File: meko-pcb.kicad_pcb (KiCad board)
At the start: 2 copper layers, 4 parts, among them IC1 ES9218PQ, U1 ESP32-MINI-1, U2 CP2102N-Axx-xQFN28, U4 CP2102N-Axx-xQFN20

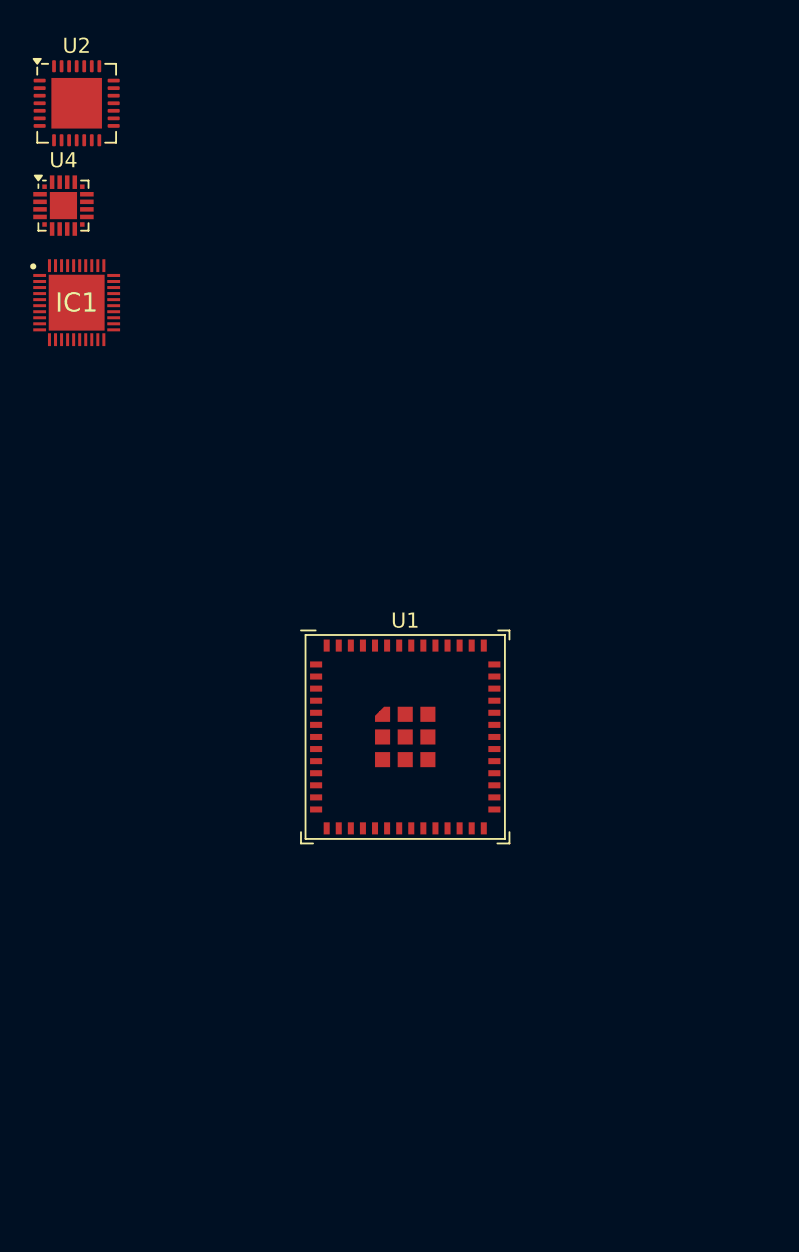
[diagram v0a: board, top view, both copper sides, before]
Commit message: added hall effect encoder
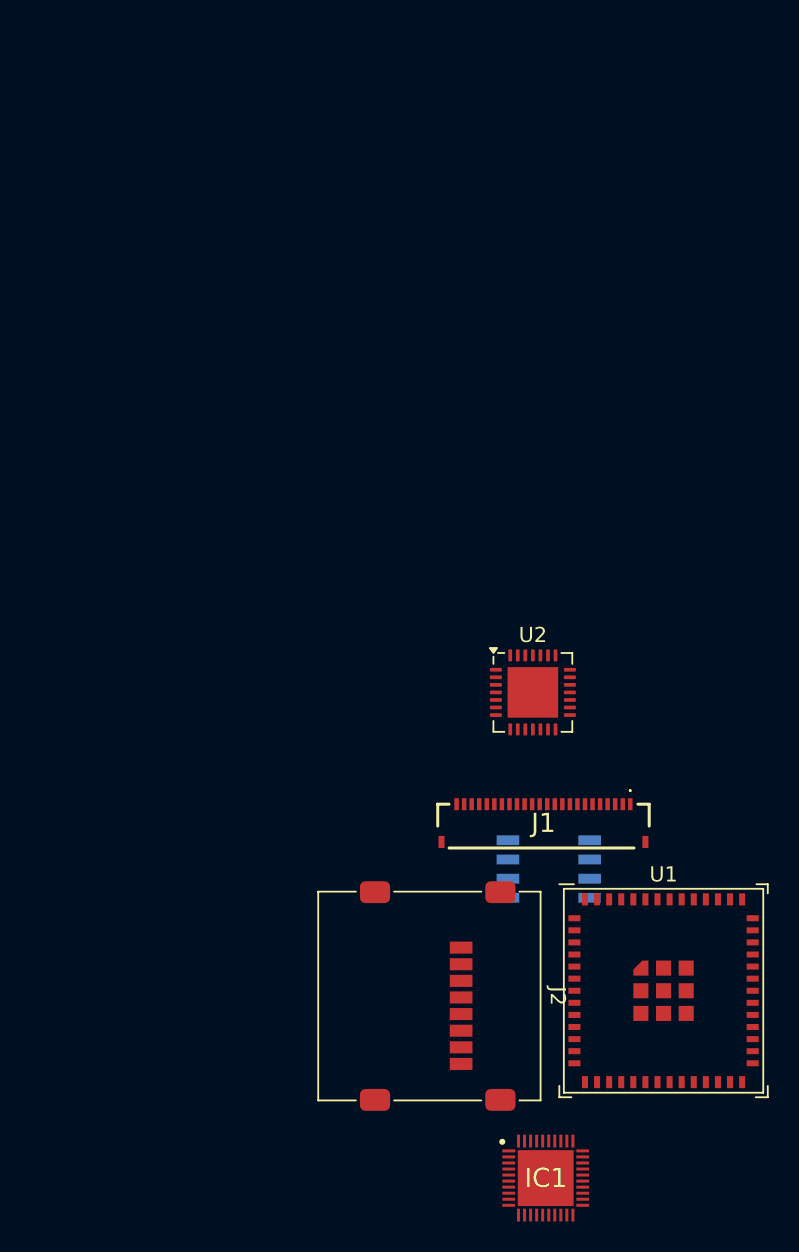
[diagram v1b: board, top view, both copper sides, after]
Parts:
- removed U4: CP2102N-Axx-xQFN20, Package_DFN_QFN:SiliconLabs_QFN-20-1EP_3x3mm_P0.5mm_EP1.8x1.8mm
- added IC2: AS5600-ASOM, AS5600-ASOM:SOIC127P600X175-8N, B.Cu at (166.3, 120.2)
- added J1: FH34SRJ-24S-0.5SH_99_, FH34SRJ-24S-0.5SH(99):FH34SRJ24S05SH99, F.Cu at (165.9, 117.3)
- added J2: Micro_SD_Card, Connector_Card:microSD_HC_Molex_47219-2001, F.Cu at (158.4, 128.6)
- IC1: footprint footprint:QFN40P500X500X80-41N-D -> ES9218PQ:QFN40P500X500X80-41N-D
- moved IC1 65.7 mm to (166.1, 140.7)
- moved U2 49.3 mm to (165.2, 108.5)
- moved U1 24.0 mm to (173.9, 128.2)

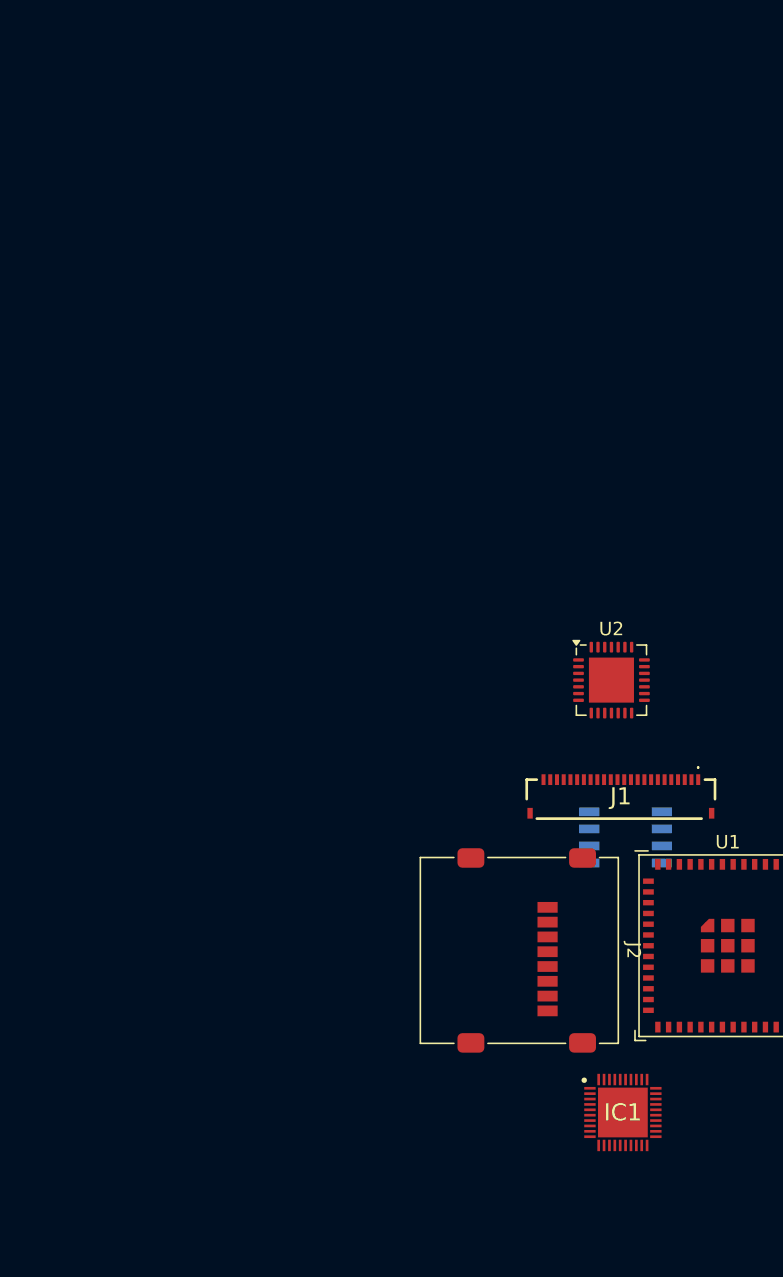
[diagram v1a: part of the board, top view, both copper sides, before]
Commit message: changed the switch converter to a LDOs
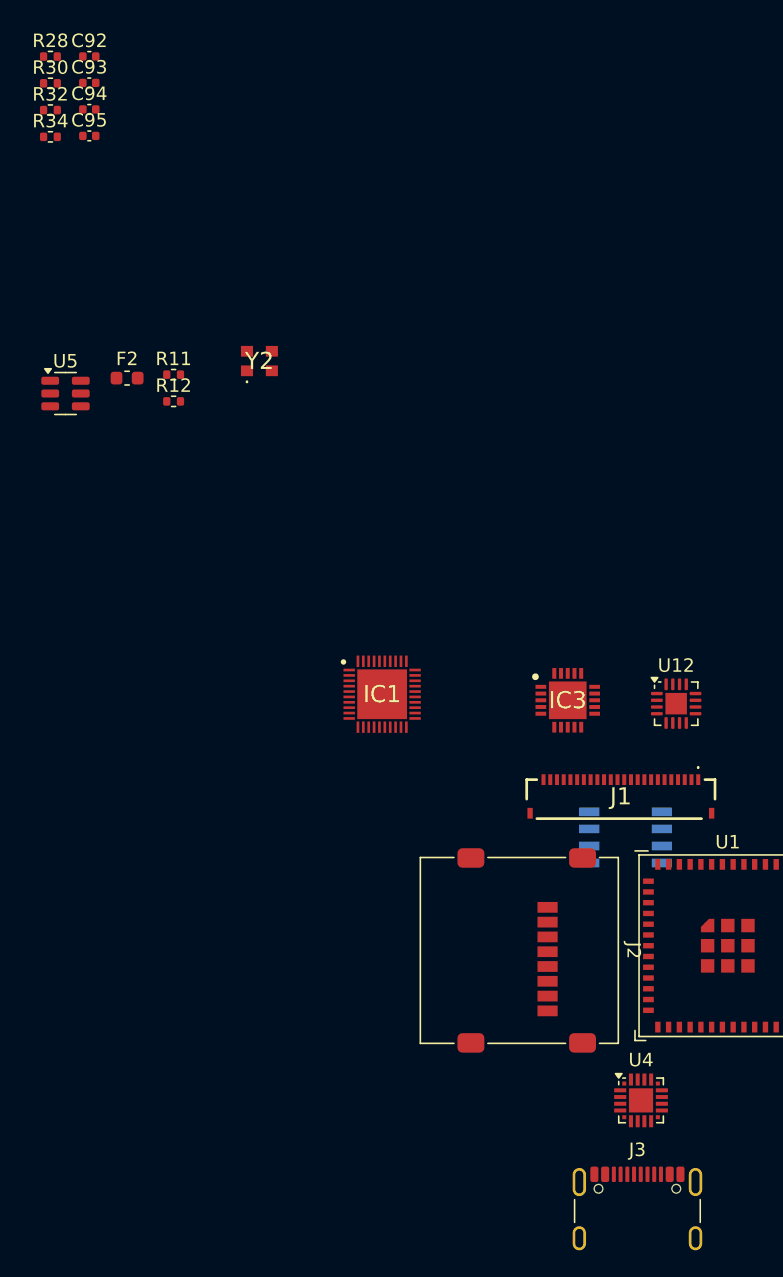
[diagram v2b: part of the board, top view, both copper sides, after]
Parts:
- removed U2: CP2102N-Axx-xQFN28, Package_DFN_QFN:QFN-28-1EP_5x5mm_P0.5mm_EP3.35x3.35mm
- added C92: 4.7uF, Capacitor_SMD:C_0402_1005Metric, F.Cu at (126.4, 62.1)
- added C93: 4.7uF, Capacitor_SMD:C_0402_1005Metric, F.Cu at (126.4, 64.1)
- added C94: 4.7uF, Capacitor_SMD:C_0402_1005Metric, F.Cu at (126.4, 66.1)
- added C95: 4.7uF, Capacitor_SMD:C_0402_1005Metric, F.Cu at (126.4, 68.0)
- added F2: 500mA, Fuse:Fuse_0603_1608Metric, F.Cu at (129.2, 86.0)
- added IC3: TPS7A8701RTJT, TPS7A8701RTJT:QFN50P400X400X80-21N-D, F.Cu at (162.0, 110.0)
- added J3: USB_C_Receptacle_USB2.0_16P, Connector_USB:USB_C_Receptacle_GCT_USB4105-xx-A_16P_TopMnt_Horizontal, F.Cu at (167.2, 148.9)
- added R11: 5.1k, Resistor_SMD:R_0402_1005Metric, F.Cu at (132.7, 85.8)
- added R12: 5.1k, Resistor_SMD:R_0402_1005Metric, F.Cu at (132.7, 87.8)
- added R28: 1.7k, Resistor_SMD:R_0402_1005Metric, F.Cu at (123.5, 62.1)
- added R30: 1.5k, Resistor_SMD:R_0402_1005Metric, F.Cu at (123.5, 64.1)
- added R32: 47k, Resistor_SMD:R_0402_1005Metric, F.Cu at (123.5, 66.1)
- added R34: 10k, Resistor_SMD:R_0402_1005Metric, F.Cu at (123.5, 68.1)
- added U12: BQ24075RGT, Package_DFN_QFN:VQFN-16-1EP_3x3mm_P0.5mm_EP1.6x1.6mm, F.Cu at (170.1, 110.2)
- added U4: CP2102N-Axx-xQFN20, Package_DFN_QFN:SiliconLabs_QFN-20-1EP_3x3mm_P0.5mm_EP1.8x1.8mm, F.Cu at (167.4, 139.8)
- added U5: USBLC6-2SC6, Package_TO_SOT_SMD:SOT-23-6, F.Cu at (124.7, 87.2)
- added Y2: ECS-2520SMV-500-GP-TR, ECS-2520SMV-500-GP-TR:ECS2520SMV500GPTR, F.Cu at (139.1, 84.8)
- moved IC1 35.9 mm to (148.2, 109.5)
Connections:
- IC1 pad 1: unconnected-(IC1-RT1-Pad1) -> GND
- IC1 pad 10: unconnected-(IC1-GSN_R-Pad10) -> GND
- IC1 pad 11: unconnected-(IC1-AGND_2-Pad11) -> GND
- IC1 pad 12: unconnected-(IC1-AGND_3-Pad12) -> GND
- IC1 pad 13: unconnected-(IC1-PNEG-Pad13) -> /audio/PNEG
- IC1 pad 14: unconnected-(IC1-PNEG_VC-Pad14) -> /audio/PNEG_VC
- IC1 pad 15: unconnected-(IC1-C2-Pad15) -> /audio/C2
- IC1 pad 16: unconnected-(IC1-C2_VC-Pad16) -> /audio/C2_VC
- IC1 pad 17: unconnected-(IC1-C1_VC-Pad17) -> /audio/C1_VC
- IC1 pad 18: unconnected-(IC1-C1-Pad18) -> /audio/C1
- IC1 pad 19: unconnected-(IC1-AVCC18-Pad19) -> +1V8
- IC1 pad 20: unconnected-(IC1-AVCC33-Pad20) -> +3V3
- IC1 pad 21: unconnected-(IC1-GSN_L-Pad21) -> GND
- IC1 pad 22: unconnected-(IC1-OUT_L-Pad22) -> Net-(IC1-OUT_L)
- IC1 pad 23: unconnected-(IC1-IN_L-Pad23) -> Net-(IC1-IN_L)
- IC1 pad 24: unconnected-(IC1-INB_L-Pad24) -> Net-(IC1-INB_L)
- IC1 pad 26: unconnected-(IC1-AGND_4-Pad26) -> GND
- IC1 pad 27: unconnected-(IC1-AVCC_DAC-Pad27) -> /audio/AVCC_DAC
- IC1 pad 28: unconnected-(IC1-VREF-Pad28) -> /audio/VREF
- IC1 pad 29: unconnected-(IC1-AVDD-Pad29) -> +1V8
- IC1 pad 3: unconnected-(IC1-XI-Pad3) -> /audio/XI
- IC1 pad 30: unconnected-(IC1-DGND_1-Pad30) -> GND
- IC1 pad 31: unconnected-(IC1-DVDD-Pad31) -> /audio/DVDD
- IC1 pad 4: unconnected-(IC1-VCCA-Pad4) -> +3V3
- IC1 pad 40: unconnected-(IC1-ADDR-Pad40) -> GND
- IC1 pad 41: unconnected-(IC1-DGND_2-Pad41) -> GND
- IC1 pad 5: unconnected-(IC1-AGND_1-Pad5) -> GND
- IC1 pad 7: unconnected-(IC1-INB_R-Pad7) -> Net-(IC1-INB_R)
- IC1 pad 8: unconnected-(IC1-IN_R-Pad8) -> Net-(IC1-IN_R)
- IC1 pad 9: unconnected-(IC1-OUT_R-Pad9) -> Net-(IC1-OUT_R)
- U1 pad 1: Net-(U1-GND-Pad1) -> GND
- U1 pad 2: Net-(U1-GND-Pad1) -> GND
- U1 pad 27: Net-(U1-GND-Pad1) -> GND
- U1 pad 38: Net-(U1-GND-Pad1) -> GND
- U1 pad 39: Net-(U1-GND-Pad1) -> GND
- U1 pad 40: Net-(U1-GND-Pad1) -> GND
- U1 pad 41: Net-(U1-GND-Pad1) -> GND
- U1 pad 42: Net-(U1-GND-Pad1) -> GND
- U1 pad 43: Net-(U1-GND-Pad1) -> GND
- U1 pad 44: Net-(U1-GND-Pad1) -> GND
- U1 pad 45: Net-(U1-GND-Pad1) -> GND
- U1 pad 46: Net-(U1-GND-Pad1) -> GND
- U1 pad 47: Net-(U1-GND-Pad1) -> GND
- U1 pad 48: Net-(U1-GND-Pad1) -> GND
- U1 pad 49: Net-(U1-GND-Pad1) -> GND
- U1 pad 50: Net-(U1-GND-Pad1) -> GND
- U1 pad 51: Net-(U1-GND-Pad1) -> GND
- U1 pad 52: Net-(U1-GND-Pad1) -> GND
- U1 pad 53: Net-(U1-GND-Pad1) -> GND
- U1 pad 54: Net-(U1-GND-Pad1) -> GND
- U1 pad 55: Net-(U1-GND-Pad1) -> GND

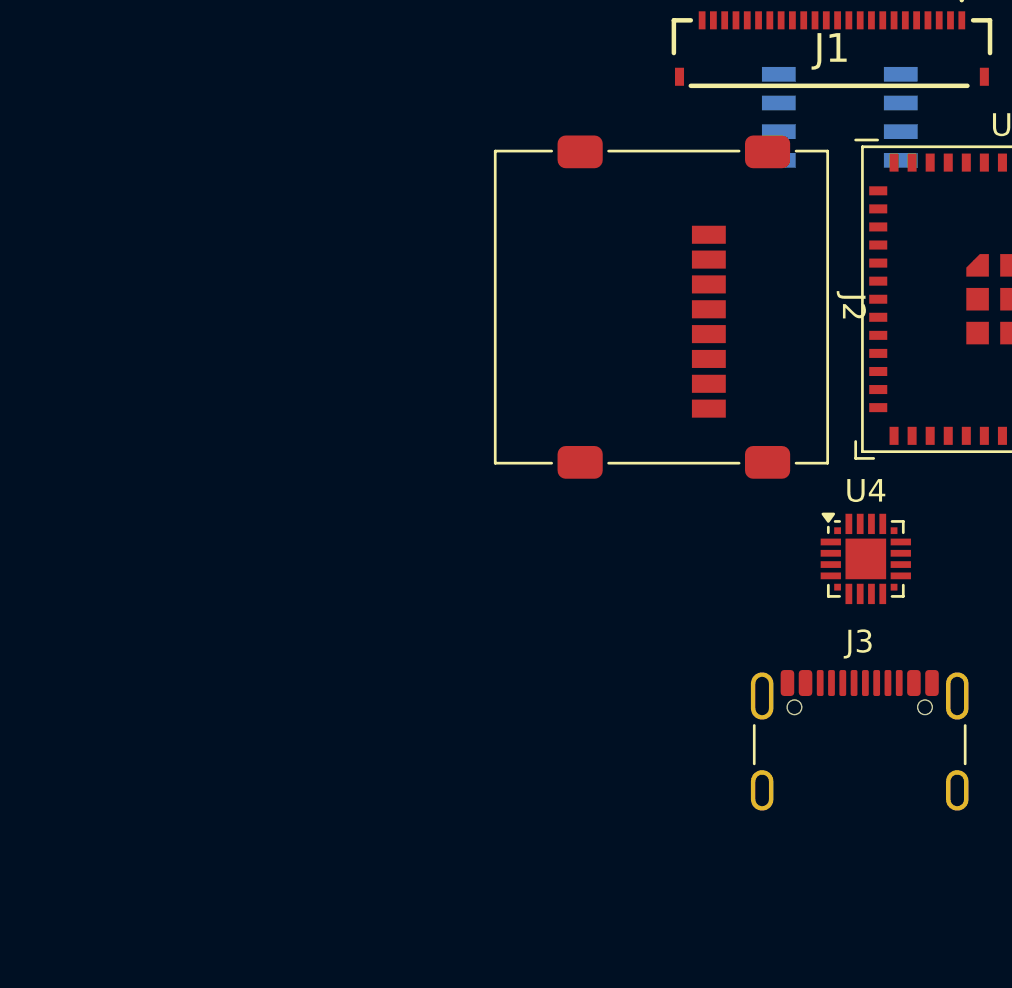
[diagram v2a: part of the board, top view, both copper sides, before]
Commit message: added the sd card slot
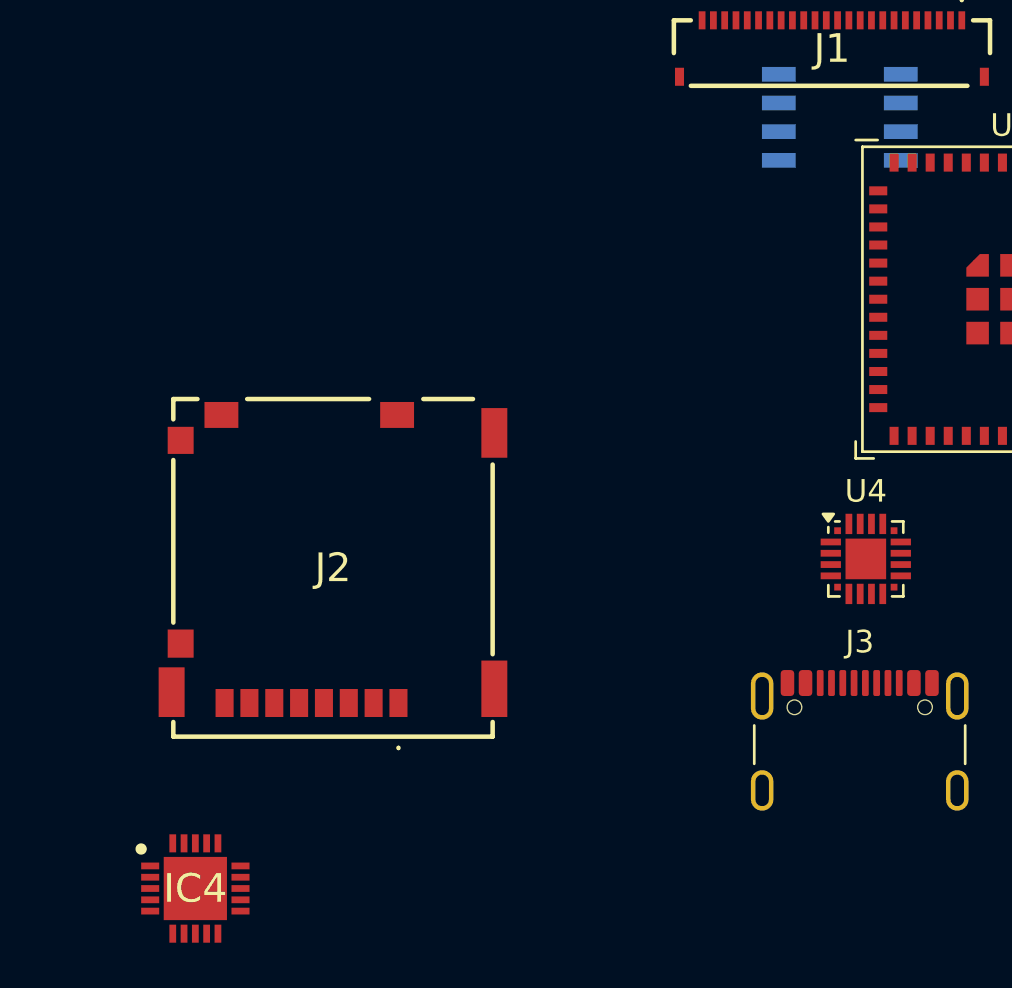
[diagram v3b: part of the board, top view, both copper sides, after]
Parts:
- added IC4: TPS7A8701RTJT, TPS7A8701RTJT:QFN50P400X400X80-21N-D, F.Cu at (137.8, 154.3)
- J2: value Micro_SD_Card -> MEM2090-00-145-00-A; footprint Connector_Card:microSD_HC_Molex_47219-2001 -> MEM2090-00-145-00-A:MEM20900014500A
- moved J2 18.6 mm to (143.9, 140.1), turned to 0 degrees
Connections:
- IC1 pad 32: unconnected-(IC1-GPIO2-Pad32) -> /audio/GPIO2
- IC1 pad 33: unconnected-(IC1-GPIO1-Pad33) -> /audio/GPIO1
- IC1 pad 34: unconnected-(IC1-DATA_2-Pad34) -> /audio/DATA_2
- IC1 pad 35: unconnected-(IC1-DATA1-Pad35) -> /audio/DATA1
- IC1 pad 36: unconnected-(IC1-DATA_CLK-Pad36) -> /audio/DATA_CLK
- IC1 pad 37: unconnected-(IC1-RESETB-Pad37) -> /audio/RESETB
- IC1 pad 38: unconnected-(IC1-SCL-Pad38) -> /audio/SCL
- IC1 pad 39: unconnected-(IC1-SDA-Pad39) -> /audio/SDA

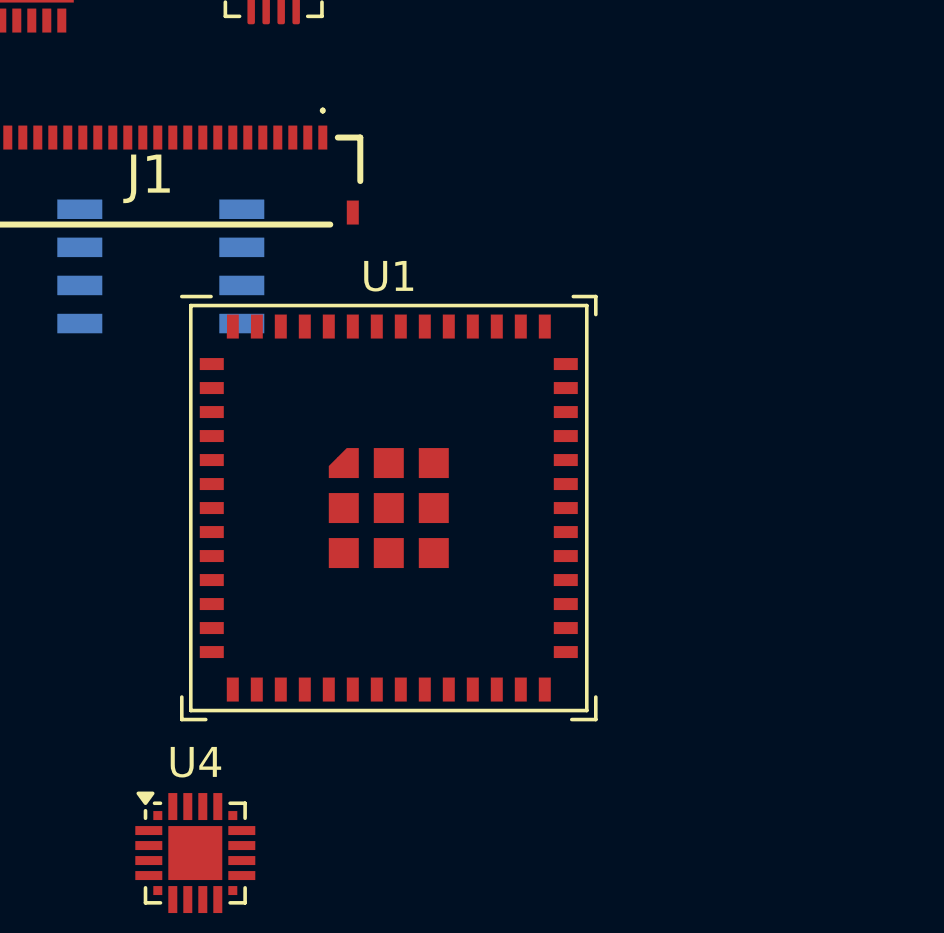
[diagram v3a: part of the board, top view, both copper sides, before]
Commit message: switched form mini esp32 to pico
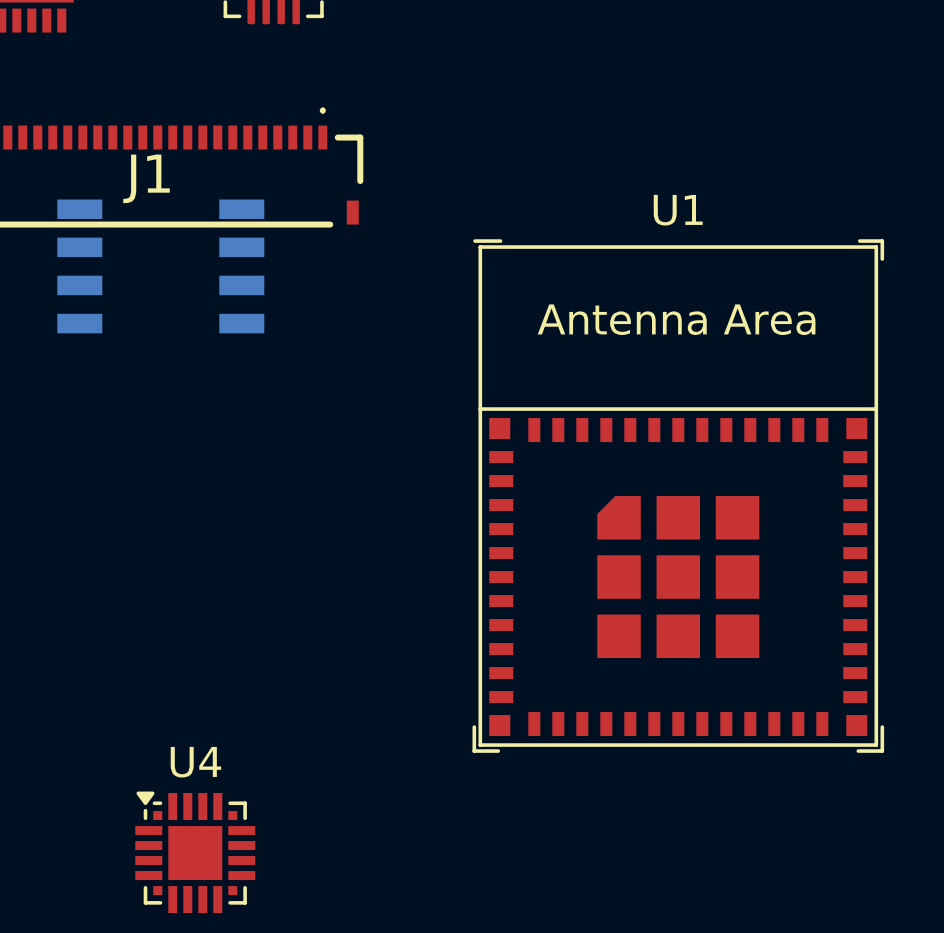
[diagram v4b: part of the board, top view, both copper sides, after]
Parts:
- U1: value ESP32-MINI-1 -> ESP32-PICO-MINI-02; footprint PCM_Espressif:ESP32-MINI-1U -> PCM_Espressif:ESP32-PICO-MINI-02
- moved U1 9.92 mm to (183.6, 130.6)
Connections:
- U1 pad 1: GND -> Net-(U1-GND-Pad1)
- U1 pad 11: unconnected-(U1-32K_XP/GPIO32/ADC1_CH4-Pad11) -> Net-(U1-GND-Pad1)
- U1 pad 14: unconnected-(U1-GPIO26/ADC2_CH9/DAC_2-Pad14) -> Net-(U1-GND-Pad1)
- U1 pad 2: GND -> Net-(U1-GND-Pad1)
- U1 pad 27: GND -> unconnected-(U1-SD_DATA_0/GPIO7-Pad27)
- U1 pad 36: unconnected-(U1-U0TXD/GPIO1-Pad36) -> Net-(U1-GND-Pad1)
- U1 pad 37: unconnected-(U1-NC-Pad37) -> Net-(U1-GND-Pad1)
- U1 pad 38: GND -> Net-(U1-GND-Pad1)
- U1 pad 39: GND -> Net-(U1-GND-Pad1)
- U1 pad 40: GND -> Net-(U1-GND-Pad1)
- U1 pad 41: GND -> Net-(U1-GND-Pad1)
- U1 pad 42: GND -> Net-(U1-GND-Pad1)
- U1 pad 43: GND -> Net-(U1-GND-Pad1)
- U1 pad 44: GND -> Net-(U1-GND-Pad1)
- U1 pad 45: GND -> Net-(U1-GND-Pad1)
- U1 pad 46: GND -> Net-(U1-GND-Pad1)
- U1 pad 47: GND -> Net-(U1-GND-Pad1)
- U1 pad 48: GND -> Net-(U1-GND-Pad1)
- U1 pad 49: GND -> Net-(U1-GND-Pad1)
- U1 pad 50: GND -> Net-(U1-GND-Pad1)
- U1 pad 51: GND -> Net-(U1-GND-Pad1)
- U1 pad 52: GND -> Net-(U1-GND-Pad1)
- U1 pad 53: GND -> Net-(U1-GND-Pad1)
